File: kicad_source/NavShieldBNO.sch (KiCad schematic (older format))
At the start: 38 parts, among them CN1 ARDUINO_MKR, U1 BNO085, U2 BMP388

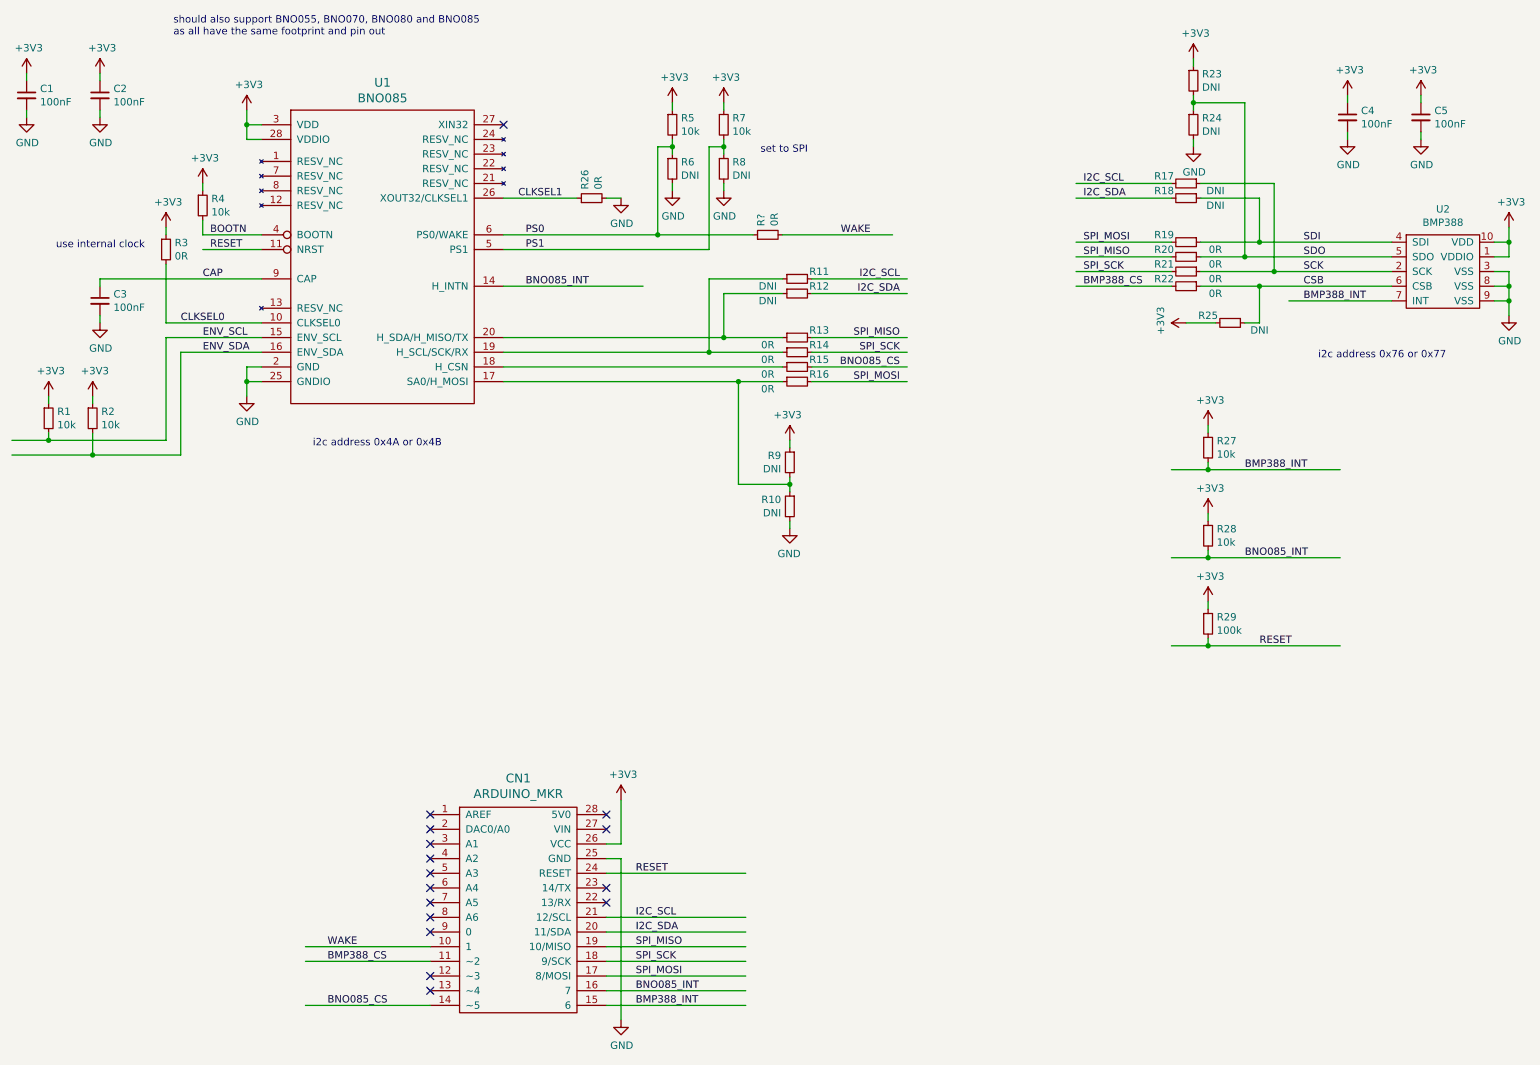
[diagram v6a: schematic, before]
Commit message: added connector for I2C and serial
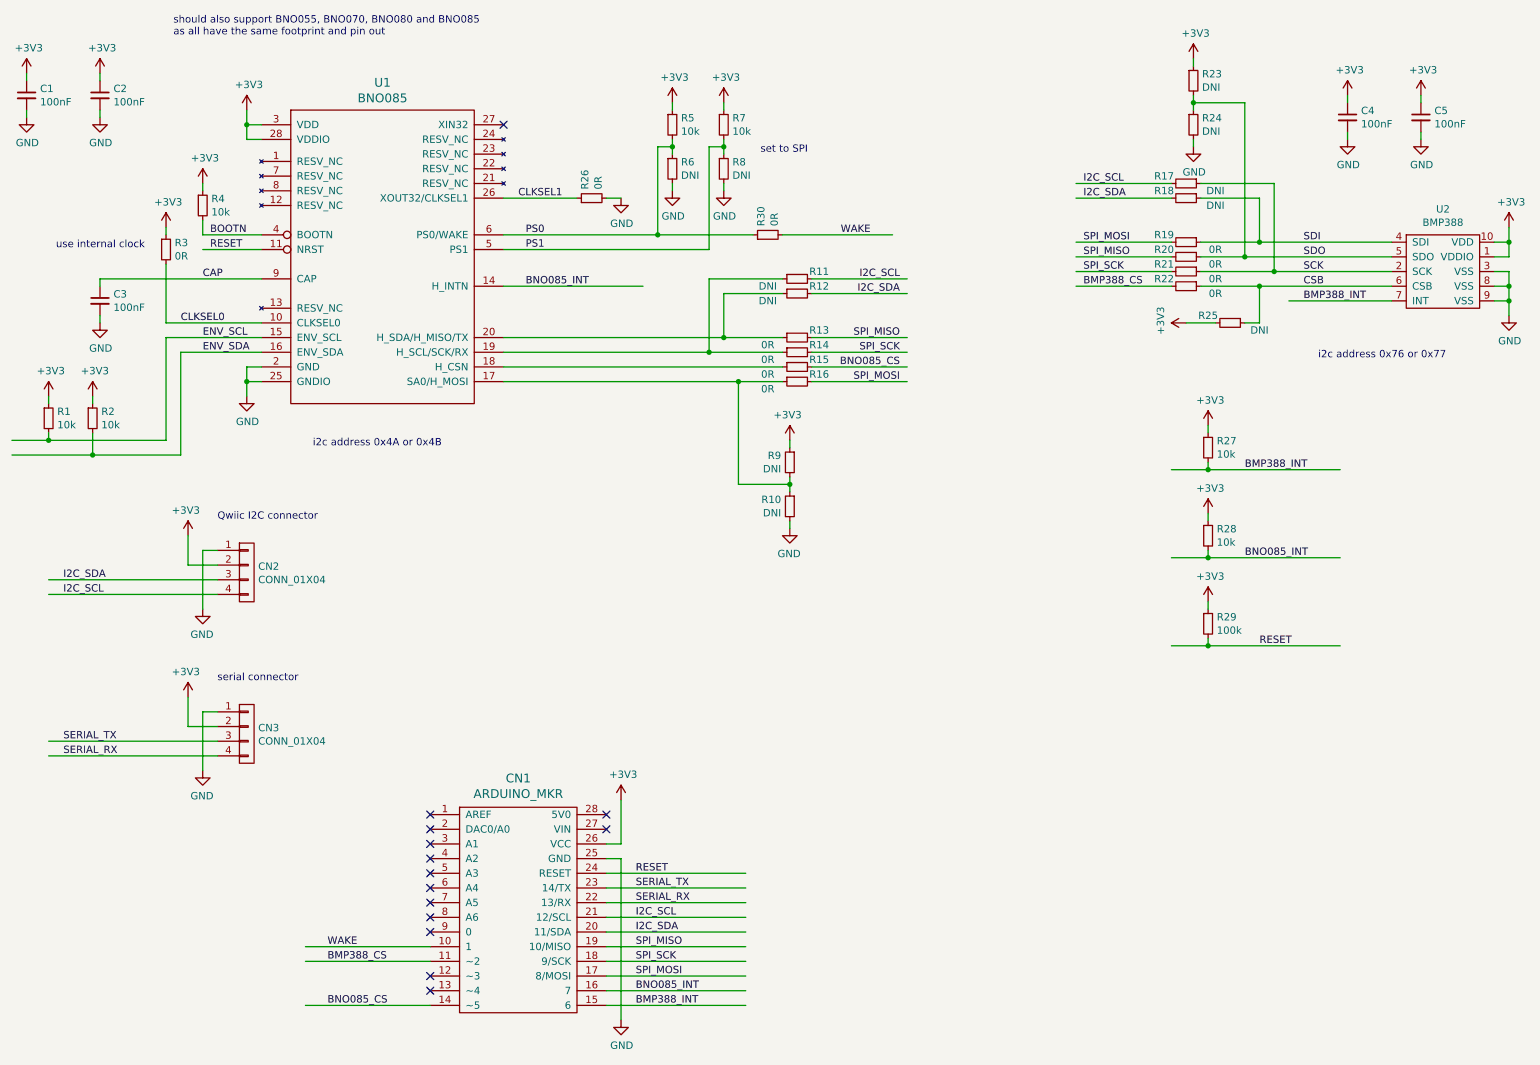
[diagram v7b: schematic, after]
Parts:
- added CN2, CN3: CONN_01X04, connectors_JST_SH:Connectors_JST_SM04B-SRSS-TB, symbol mechanical-connectors:CONN_01X04
- gave numbers to parts that had none: 1
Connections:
- net labels added: SERIAL_RX, SERIAL_TX
- wire segments 145 -> 159
- no-connect marks 16 -> 14
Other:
- note added: "Qwiic I2C connector"
- note added: "serial connector"
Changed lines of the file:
@@
 Wire Wire Line
 	5800 6400 4850 6400
-NoConn ~ 4850 6500
-NoConn ~ 4850 6600
 NoConn ~ 3650 7200
 NoConn ~ 3650 6800
@@
 	5550 1450 5550 2150
 $Comp
-L devices:R_0603 R?
+L devices:R_0603 R30
 U 1 1 5F6453B8
 P 5950 2050
-F 0 "R?" H 6009 2096 50  0000 L CNN
+F 0 "R30" H 6009 2096 50  0000 L CNN
 F 1 "0R" H 6009 2005 50  0000 L CNN
 F 2 "resistors:R_0603" H 5950 1900 50  0001 C CNN
@@
 Text Label 2950 6900 0    50   ~ 0
 WAKE
+$Comp
+L mechanical-connectors:CONN_01X04 CN2
+U 1 1 5F65BE4F
+P 2400 4350
+F 0 "CN2" H 2478 4391 50  0000 L CNN
+F 1 "CONN_01X04" H 2478 4300 50  0000 L CNN
+F 2 "connectors_JST_SH:Connectors_JST_SM04B-SRSS-TB" H 2400 4350 50  0001 C CNN
+F 3 "" H 2400 4350 50  0000 C CNN
+	1    2400 4350
+	1    0    0    -1
+$EndComp
+$Comp
+L power-supply:GND #PWR035
+U 1 1 5F65DDC3
+P 2100 4600
+F 0 "#PWR035" H 2100 4350 50  0001 C CNN
+F 1 "GND" H 2105 4427 50  0000 C CNN
+F 2 "" H 2100 4600 50  0000 C CNN
+F 3 "" H 2100 4600 50  0000 C CNN
+	1    2100 4600
+	-1   0    0    -1
+$EndComp
+$Comp
+L power-supply:+3V3 #PWR033
+U 1 1 5F65EA07
+P 2000 4100
+F 0 "#PWR033" H 2000 3950 50  0001 C CNN
+F 1 "+3V3" H 2015 4273 50  0000 C CNN
+F 2 "" H 2000 4100 50  0000 C CNN
+F 3 "" H 2000 4100 50  0000 C CNN
+	1    2000 4100
+	-1   0    0    -1
+$EndComp
+Wire Wire Line
+	2200 4300 2000 4300
+Wire Wire Line
+	2000 4300 2000 4100
+Wire Wire Line
+	2200 4200 2100 4200
+Wire Wire Line
+	2100 4200 2100 4600
+Wire Wire Line
+	1050 4400 2200 4400
+Wire Wire Line
+	1050 4500 2200 4500
+Text Label 1150 4400 0    50   ~ 0
+I2C_SDA
+Text Label 1150 4500 0    50   ~ 0
+I2C_SCL
+Text Notes 2200 4000 0    50   ~ 0
+Qwiic I2C connector
+$Comp
+L mechanical-connectors:CONN_01X04 CN3
+U 1 1 5F686AEC
+P 2400 5450
+F 0 "CN3" H 2478 5491 50  0000 L CNN
+F 1 "CONN_01X04" H 2478 5400 50  0000 L CNN
+F 2 "connectors_JST_SH:Connectors_JST_SM04B-SRSS-TB" H 2400 5450 50  0001 C CNN
+F 3 "" H 2400 5450 50  0000 C CNN
+	1    2400 5450
+	1    0    0    -1
+$EndComp
+$Comp
+L power-supply:GND #PWR036
+U 1 1 5F686AF6
+P 2100 5700
+F 0 "#PWR036" H 2100 5450 50  0001 C CNN
+F 1 "GND" H 2105 5527 50  0000 C CNN
+F 2 "" H 2100 5700 50  0000 C CNN
+F 3 "" H 2100 5700 50  0000 C CNN
+	1    2100 5700
+	-1   0    0    -1
+$EndComp
+$Comp
+L power-supply:+3V3 #PWR034
+U 1 1 5F686B00
+P 2000 5200
+F 0 "#PWR034" H 2000 5050 50  0001 C CNN
+F 1 "+3V3" H 2015 5373 50  0000 C CNN
+F 2 "" H 2000 5200 50  0000 C CNN
+F 3 "" H 2000 5200 50  0000 C CNN
+	1    2000 5200
+	-1   0    0    -1
+$EndComp
+Wire Wire Line
+	2200 5400 2000 5400
+Wire Wire Line
+	2000 5400 2000 5200
+Wire Wire Line
+	2200 5300 2100 5300
+Wire Wire Line
+	2100 5300 2100 5700
+Wire Wire Line
+	1050 5500 2200 5500
+Wire Wire Line
+	1050 5600 2200 5600
+Text Notes 2200 5100 0    50   ~ 0
+serial connector
+Wire Wire Line
+	5800 6500 4850 6500
+Wire Wire Line
+	5800 6600 4850 6600
+Text Label 5050 6500 0    50   ~ 0
+SERIAL_TX
+Text Label 5050 6600 0    50   ~ 0
+SERIAL_RX
+Text Label 1150 5600 0    50   ~ 0
+SERIAL_RX
+Text Label 1150 5500 0    50   ~ 0
+SERIAL_TX
 $EndSCHEMATC

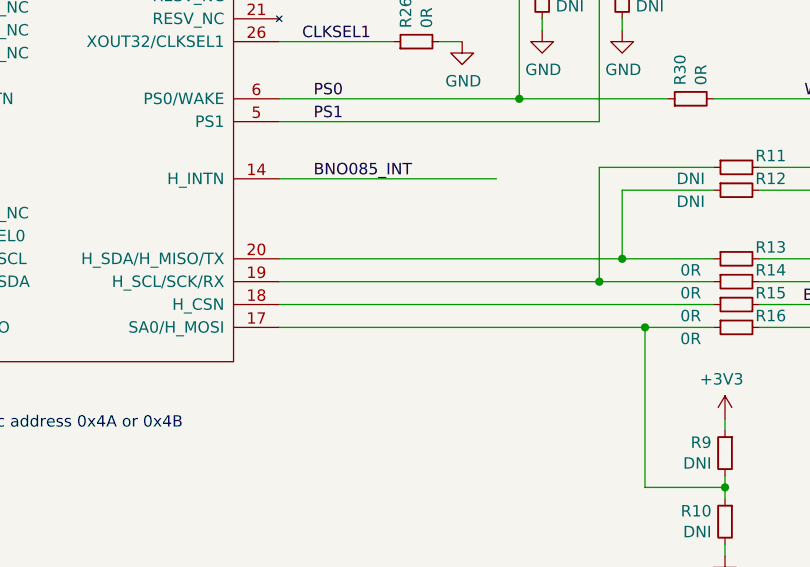
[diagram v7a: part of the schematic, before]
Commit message: made pcb bigger and added holes for Arduino MKR
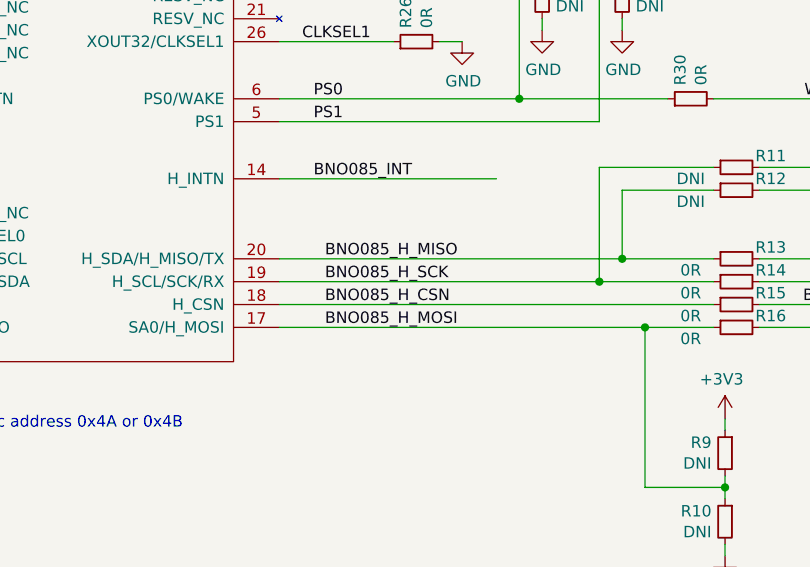
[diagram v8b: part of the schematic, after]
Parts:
- CN1: footprint MODULE_compute:ARDUINO_MKR -> MODULE_compute:ARDUINO_MKR_HOLES
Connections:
- net labels added: BNO085_H_CSN, BNO085_H_MISO, BNO085_H_MOSI, BNO085_H_SCK
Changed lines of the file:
@@
 F 0 "CN1" H 4250 7547 60  0000 C CNN
 F 1 "ARDUINO_MKR" H 4250 7441 60  0000 C CNN
-F 2 "MODULE_compute:ARDUINO_MKR" H 4150 7300 60  0001 C CNN
+F 2 "MODULE_compute:ARDUINO_MKR_HOLES" H 4150 7300 60  0001 C CNN
 F 3 "" H 4250 6350 60  0000 C CNN
 	1    4250 6650
@@
 Text Label 1150 5500 0    50   ~ 0
 SERIAL_TX
+Text Label 4350 2950 0    50   ~ 0
+BNO085_H_CSN
+Text Label 4350 3050 0    50   ~ 0
+BNO085_H_MOSI
+Text Label 4350 2850 0    50   ~ 0
+BNO085_H_SCK
+Text Label 4350 2750 0    50   ~ 0
+BNO085_H_MISO
 $EndSCHEMATC
